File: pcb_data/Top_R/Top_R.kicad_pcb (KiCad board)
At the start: 2 copper layers, 186.9 x 96.4 mm, 103 parts, among them J1 Conn_01x02, U1 XIAO-nRF52840

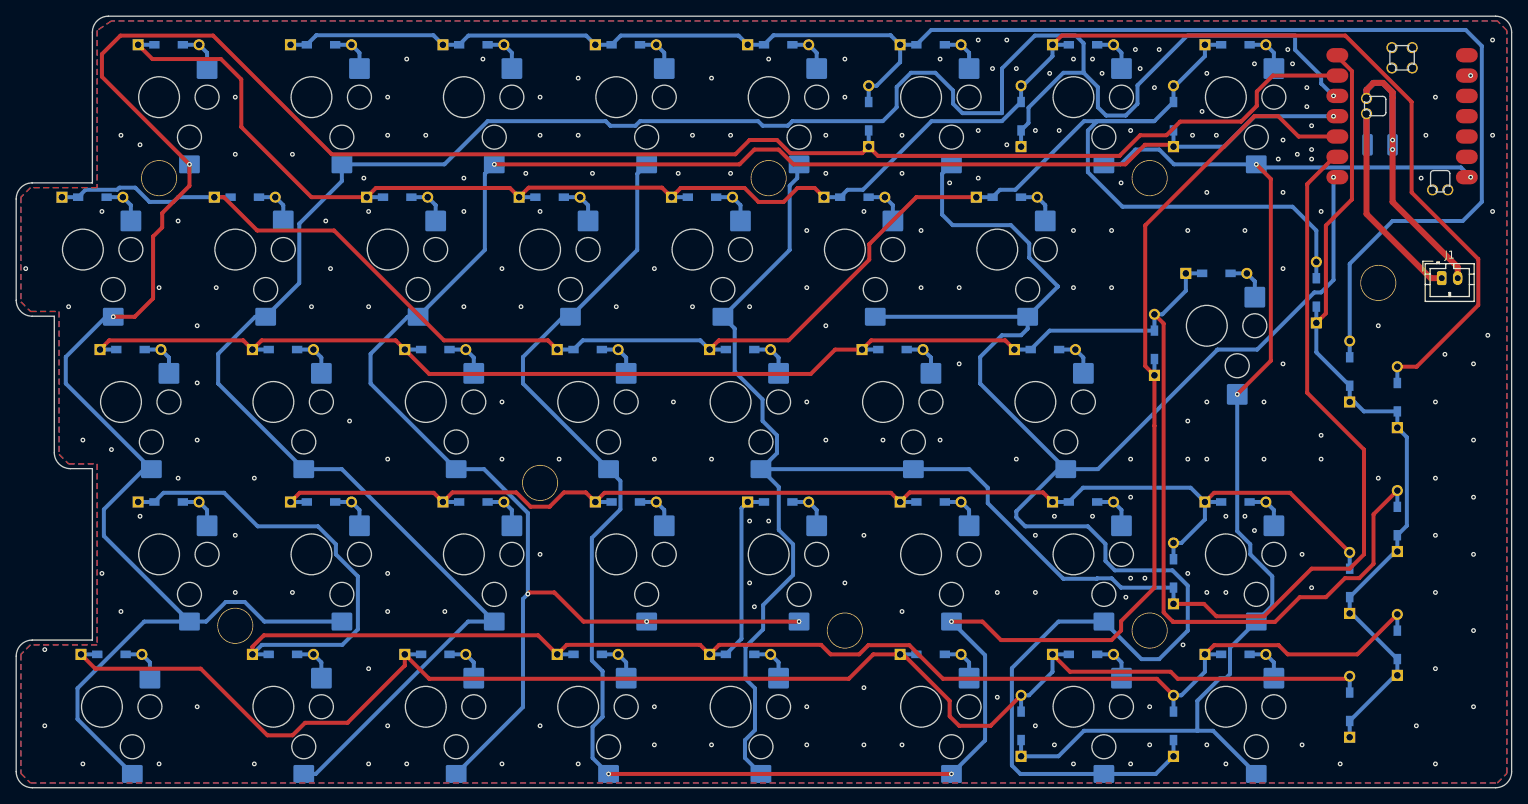
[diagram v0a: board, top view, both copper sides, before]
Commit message: remove zone, segment and via
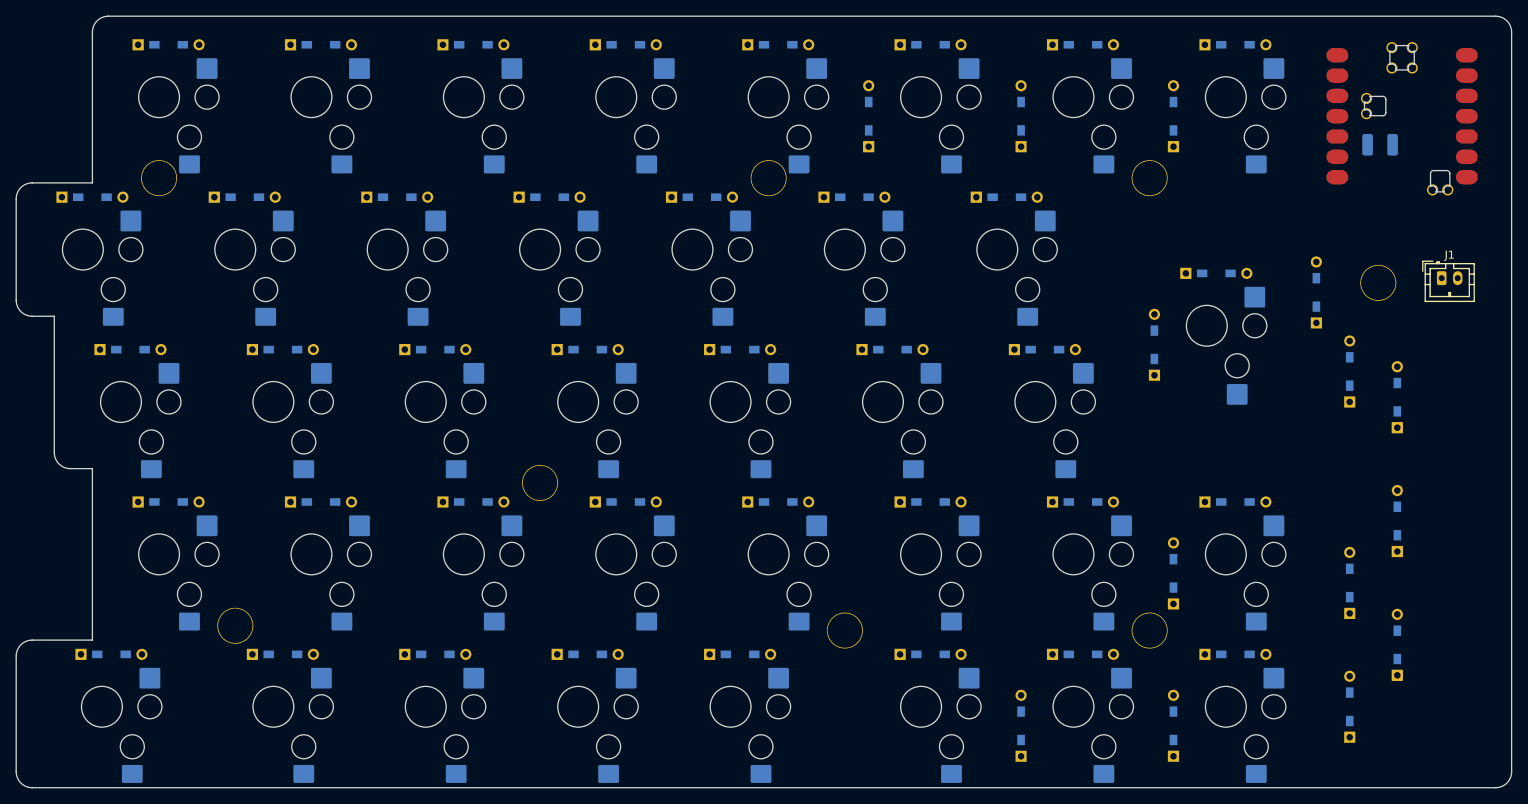
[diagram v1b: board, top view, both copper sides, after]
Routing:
- net IO 7: track 318.6 -> 0.00 mm, vias 2 -> 0
- net IO 8: track 286.5 -> 0.00 mm, vias 1 -> 0
- net IO 10: track 264.8 -> 0.00 mm, vias 3 -> 0
- net Net-(D0-12-K): track 245.6 -> 0.00 mm
- net IO 9: track 243.9 -> 0.00 mm, vias 5 -> 0
- net Net-(D0-8-K): track 243.5 -> 0.00 mm
- net IO 12: track 238.5 -> 0.00 mm, vias 1 -> 0
- net Net-(D0-10-K): track 237.6 -> 0.00 mm
- net IO 11: track 232.4 -> 0.00 mm
- net Net-(D0-9-K): track 229.8 -> 0.00 mm
- net Net-(D1-7-K): track 214.6 -> 0.00 mm
- net Net-(D0-13-K): track 193.7 -> 0.00 mm
- net Net-(D0-11-K): track 164.4 -> 0.00 mm
- net IO 13: track 162.5 -> 0.00 mm, vias 3 -> 0
- net INTR_R: track 106.3 -> 0.00 mm
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- removed copper zone on B.Cu, net GND
- removed copper zone on F.Cu, net GND

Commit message: remove diode
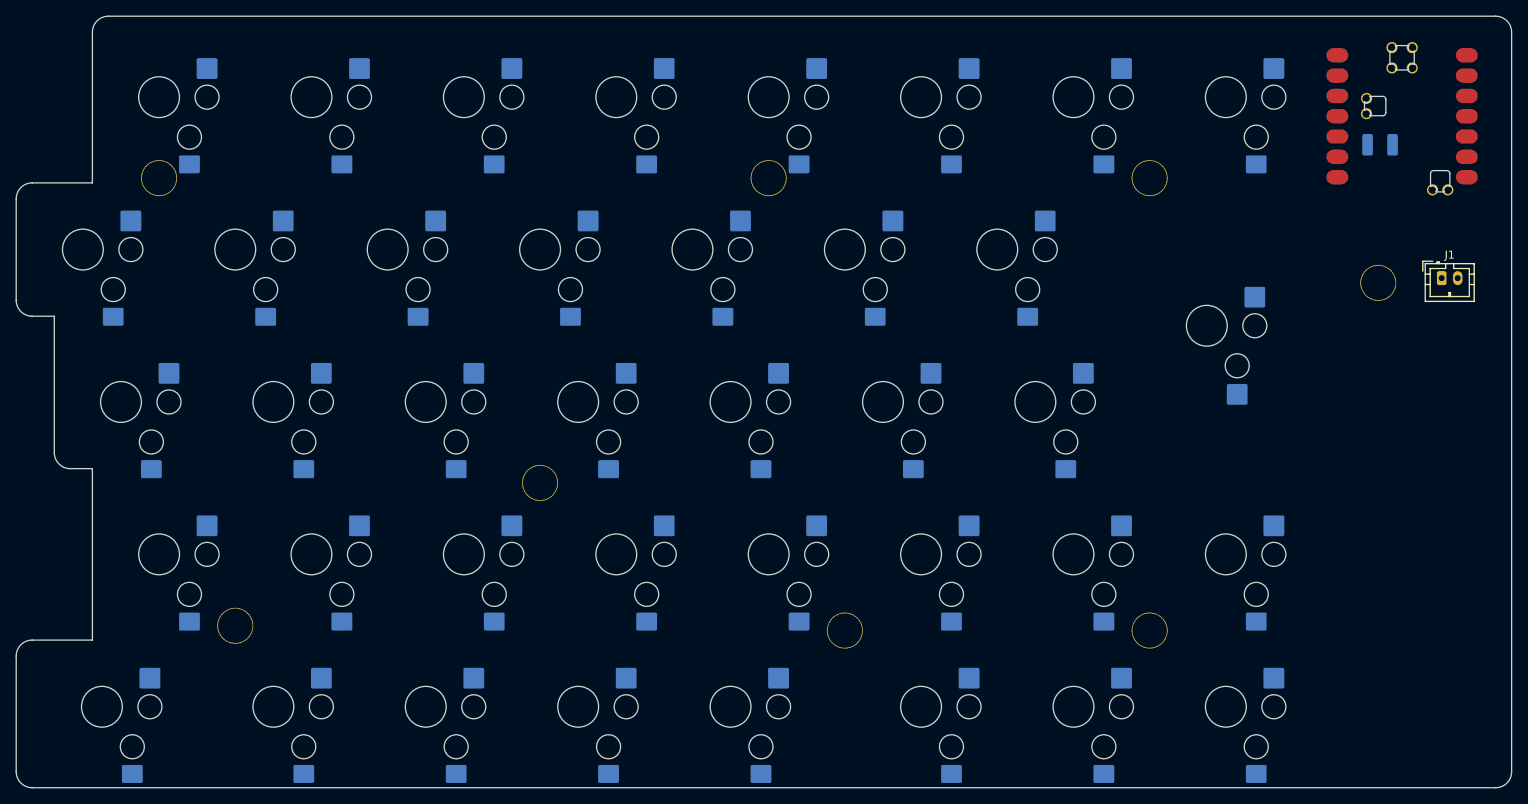
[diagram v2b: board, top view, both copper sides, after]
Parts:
- removed D0-10, D0-11, D0-12, D0-13, D0-8, D0-9, D1-10, D1-11, D1-12, D1-7, D1-9, D2-10, D2-11, D2-12, D2-13, D2-7, D2-8, D3-11, D3-12, D3-13, D3-7, D3-8, D3-9, D4-10, D4-12, D4-7, D4-8, D4-9, D5-10, D5-11, D5-13, D5-7, D5-8, D5-9, D6-10, D6-11, D6-12, D6-8, D6-9, DI10, DI11, DI12, DI13, DI7, DI8, DI9, DS10, DS11, DS12, DS13, DS7, DS8, DS9: 1N4148W, kbd_Parts:Diode_TH_SMD

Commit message: replace switch footprint
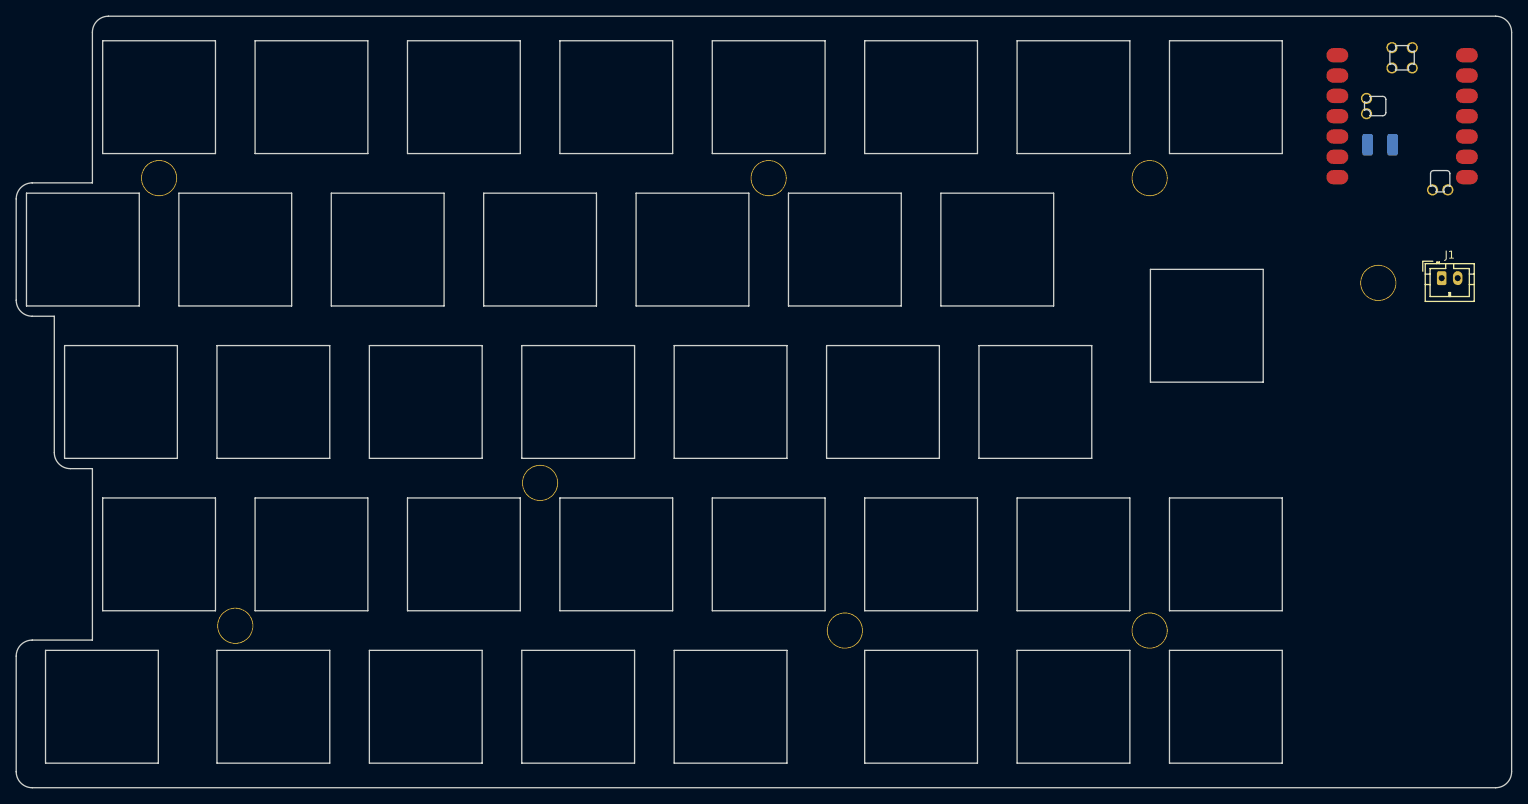
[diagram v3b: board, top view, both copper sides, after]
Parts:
- RC0-10, RC0-11, RC0-12, RC0-8, RC0-9, RC1-10, RC1-11, RC1-12, RC1-7, RC1-9, RC2-10, RC2-11, RC2-12, RC2-13, RC2-7, RC2-8, RC3-11, RC3-12, RC3-13, RC3-7, RC3-8, RC3-9, RC4-10, RC4-12, RC4-7, RC4-8, RC4-9, RC5-10, RC5-11, RC5-13, RC5-7, RC5-8, RC5-9, RC6-11, RC6-12, RC6-8, RC6-9: footprint custom-library:Kailh-PG1353-Hotswap-R-1U -> kbd_SW_Hole:SW_Hole_1u
- RC0-13: footprint custom-library:Kailh-PG1353-Hotswap-R-1.25U -> kbd_SW_Hole:SW_Hole_1.25u
- RC6-10: footprint custom-library:Kailh-PG1353-Hotswap-ISOEnter-R -> custom-library:SW_Hole_ISOEnter

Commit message: update line
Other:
- board size 186.9 x 96.4 mm -> 163.1 x 96.4 mm
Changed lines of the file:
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@@
 	)
 	(gr_line
-		(start 250.412712 143.470433)
+		(start 226.6000 143.470433)
 		(end 67.48443 143.470433)
 		(stroke
@@
 	)
 	(gr_line
-		(start 250.412712 47.029727)
+		(start 226.6000 47.029727)
 		(end 77.009438 47.029727)
 		(stroke
@@
 	)
 	(gr_arc
-		(start 250.412712 47.029727)
-		(mid 251.826926 47.615513)
-		(end 252.412712 49.029727)
+		(start 226.6000 47.029727)
+		(mid 228.014214 47.615513)
+		(end 228.6000 49.029727)
 		(stroke
 			(width 0.05)
@@
 	)
 	(gr_arc
-		(start 252.412712 141.470433)
-		(mid 251.826926 142.884647)
-		(end 250.412712 143.470433)
+		(start 228.6000 141.470433)
+		(mid 228.014214 142.884647)
+		(end 226.6000 143.470433)
 		(stroke
 			(width 0.05)
@@
 	)
 	(gr_line
-		(start 252.412712 49.029727)
-		(end 252.412712 141.470433)
+		(start 228.6000 49.029727)
+		(end 228.6000 141.470433)
 		(stroke
 			(width 0.05)

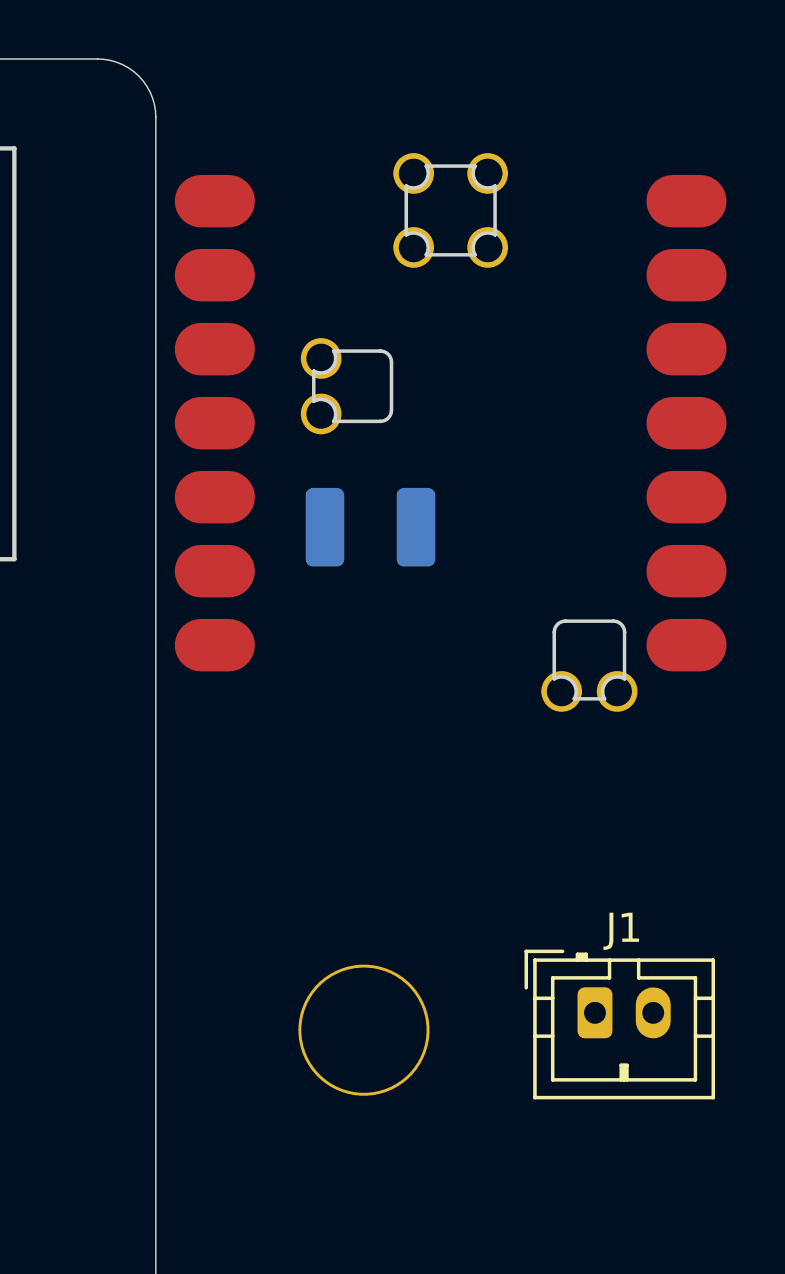
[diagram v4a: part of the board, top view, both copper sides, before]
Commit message: remove unnecessary footprint
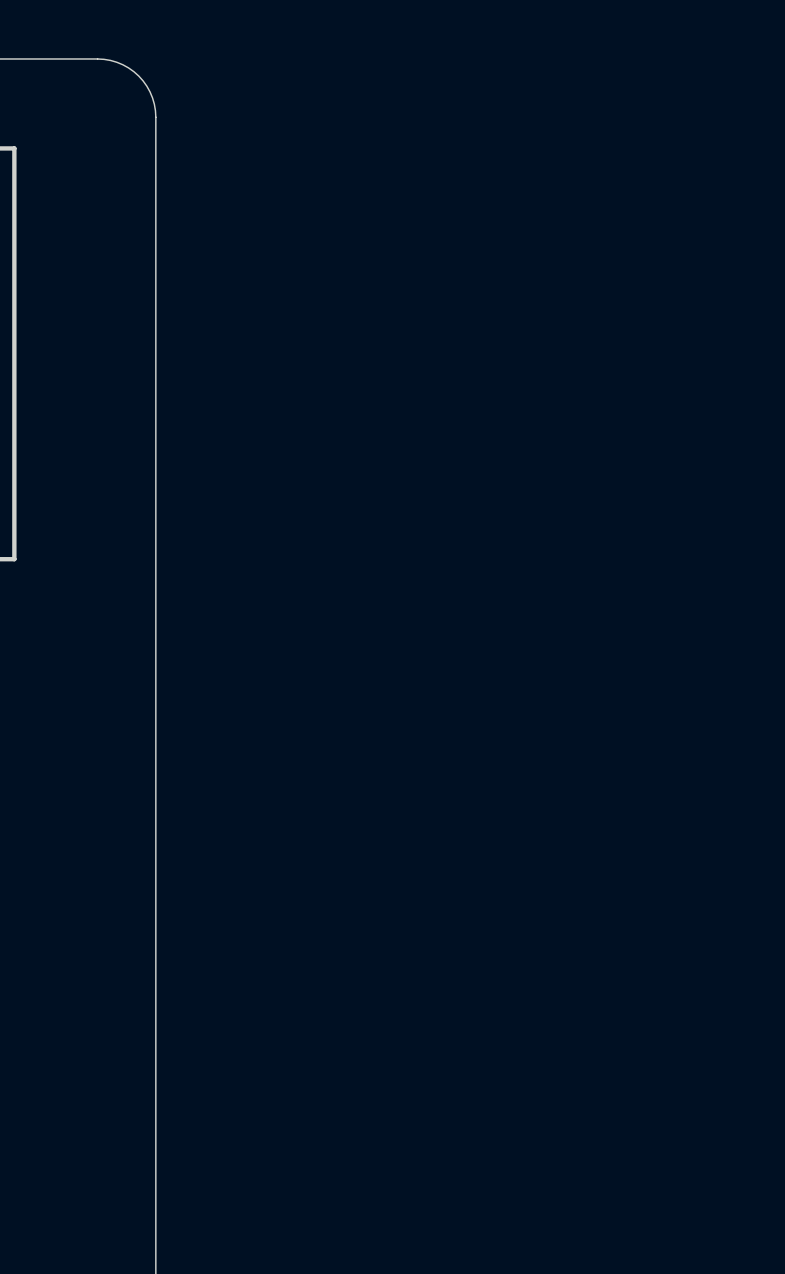
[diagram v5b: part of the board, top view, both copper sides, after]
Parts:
- removed C1: GRM32EC81C476KE15L, Capacitor_SMD:C_1210_3225Metric_Pad1.33x2.70mm_HandSolder
- removed H7: MountingHole, kbd_Hole:m2_Spacer_Hole
- removed J1: Conn_01x02, Connector_JST:JST_PH_B2B-PH-K_1x02_P2.00mm_Vertical
- removed U1: XIAO-nRF52840, mcu:xiao-ble-smd-cutout
